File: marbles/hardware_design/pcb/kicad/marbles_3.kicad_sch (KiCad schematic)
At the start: 39 parts

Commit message: replace led/button switches
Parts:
- removed SW1, SW2: (no value), symbol marbles-eagle-import:LP4OA1PBCT
- added SW1, SW2: SW_Push_LED, Supercell 1.3:C&K_D6R, symbol Switch:SW_Push_LED
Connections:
- net GND: now also SW1.1, SW1.2, SW2.1, SW2.2
- net SW_T_DV: now also SW1.4
- net SW_X_DV: now also SW2.4
- net at R1.2: now also SW1.3
- net at R5.2: now also SW2.3
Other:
- moved on the sheet: R1, R5

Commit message: added SMD LEDs in parallel with THT footprint
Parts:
- removed LED1, LED2, LED3, LED4, LED5: (no value), symbol marbles-eagle-import:LED-BICOLOR-THROUGHHOLE2.54
- added LED1, LED2, LED3, LED4, LED5: LED-BICOLOR-THROUGHHOLE, marbles:LED-BICOLOR-THROUGHHOLE-2.54, symbol marbles-eagle-import:LED-BICOLOR-THROUGHHOLE
- added LED1-2, LED2-2, LED3-2, LED4-2, LED5-2: LED_Dual_KAKA, Supercell 1.3:bicolor 0606 LED, symbol Device:LED_Dual_KAKA
- C17, C18, C24, C28, C29, C36, C38, C8: value (none) -> 100n; footprint (none) -> marbles:C0402
- R1, R5: value (none) -> 39; footprint (none) -> marbles:R0402
- R10, R12, R17, R18, R36: value (none) -> 1.5k; footprint (none) -> marbles:R0402
- R11, R15, R19, R9: value (none) -> 2.2k; footprint (none) -> marbles:R0402
- R13, R14, R16, R20, R21, R37, R38, R4: value (none) -> 10kB; footprint (none) -> marbles:ALPS_POT_VERTICAL_PS
- SW3, SW4, SW5, SW6, SW7: value (none) -> TAC_SWITCHPTH; footprint (none) -> marbles:TACTILE-PTH
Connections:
- net GND: now also LED1-2.KG, LED1-2.KR, LED1.2 (C), LED2-2.KG, LED2-2.KR, LED2.2 (C), LED3-2.KG, LED3-2.KR, LED3.2 (C), LED4-2.KG, LED4-2.KR, LED4.2 (C), LED5-2.KG, LED5.2 (C)
- net at R9.2: now also LED1-2.AR, LED1.3 (RED)
- net at R15.2: now also LED4-2.AR, LED4.3 (RED)
- net at R17.2: now also LED4-2.AG, LED4.1 (GRN)
- net at R36.2: now also LED5-2.AG, LED5.1 (GRN)
- net at R12.2: now also LED2-2.AG, LED2.1 (GRN)
- net at R11.2: now also LED2-2.AR, LED2.3 (RED)
- net at R10.2: now also LED1-2.AG, LED1.1 (GRN)
- net at R18.2: now also LED3-2.AG, LED3.1 (GRN)
- net at R19.2: now also LED3-2.AR, LED3.3 (RED)
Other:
- moved on the sheet: R10, R11, R12, R15, R17, R18, R19, R36, R9

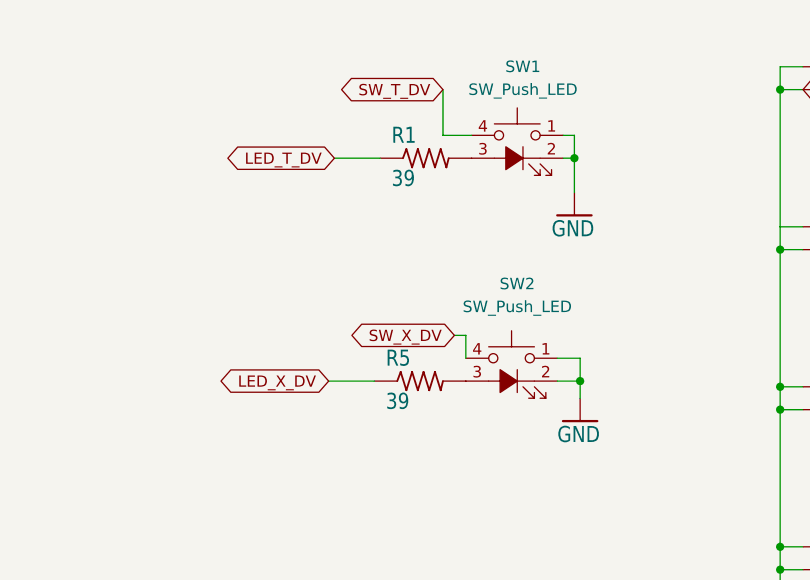
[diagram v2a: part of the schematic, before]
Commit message: change two 39 ohm 0402 resistors to 1k 0603
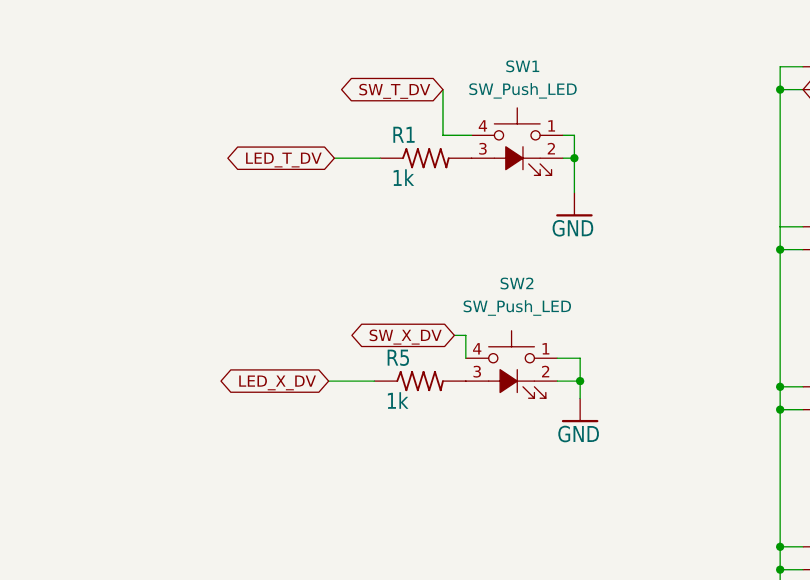
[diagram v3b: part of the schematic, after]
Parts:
- R1, R5: value 39 -> 1k; footprint marbles:R0402 -> marbles:R0603
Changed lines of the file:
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@@
       (effects (font (size 1.778 1.5113)) (justify left bottom))
     )
-    (property "Value" "39" (id 1) (at 142.24 163.322 0)
-      (effects (font (size 1.778 1.5113)) (justify left bottom))
-    )
-    (property "Footprint" "marbles:R0402" (id 2) (at 146.05 160.02 0)
+    (property "Value" "1k" (id 1) (at 142.24 163.322 0)
+      (effects (font (size 1.778 1.5113)) (justify left bottom))
+    )
+    (property "Footprint" "marbles:R0603" (id 2) (at 146.05 160.02 0)
       (effects (font (size 1.27 1.27)) hide)
     )
@@
       (effects (font (size 1.778 1.5113)) (justify left bottom))
     )
-    (property "Value" "39" (id 1) (at 141.605 188.087 0)
-      (effects (font (size 1.778 1.5113)) (justify left bottom))
-    )
-    (property "Footprint" "marbles:R0402" (id 2) (at 145.415 184.785 0)
-      (effects (font (size 1.27 1.27)) hide)
-    )
+    (property "Value" "1k" (id 1) (at 141.605 188.087 0)
+      (effects (font (size 1.778 1.5113)) (justify left bottom))
+    )
+    (property "Footprint" "marbles:R0603" (id 2) (at 145.415 184.785 0)
+      (effects (font (size 1.27 1.27)) hide)
+    )

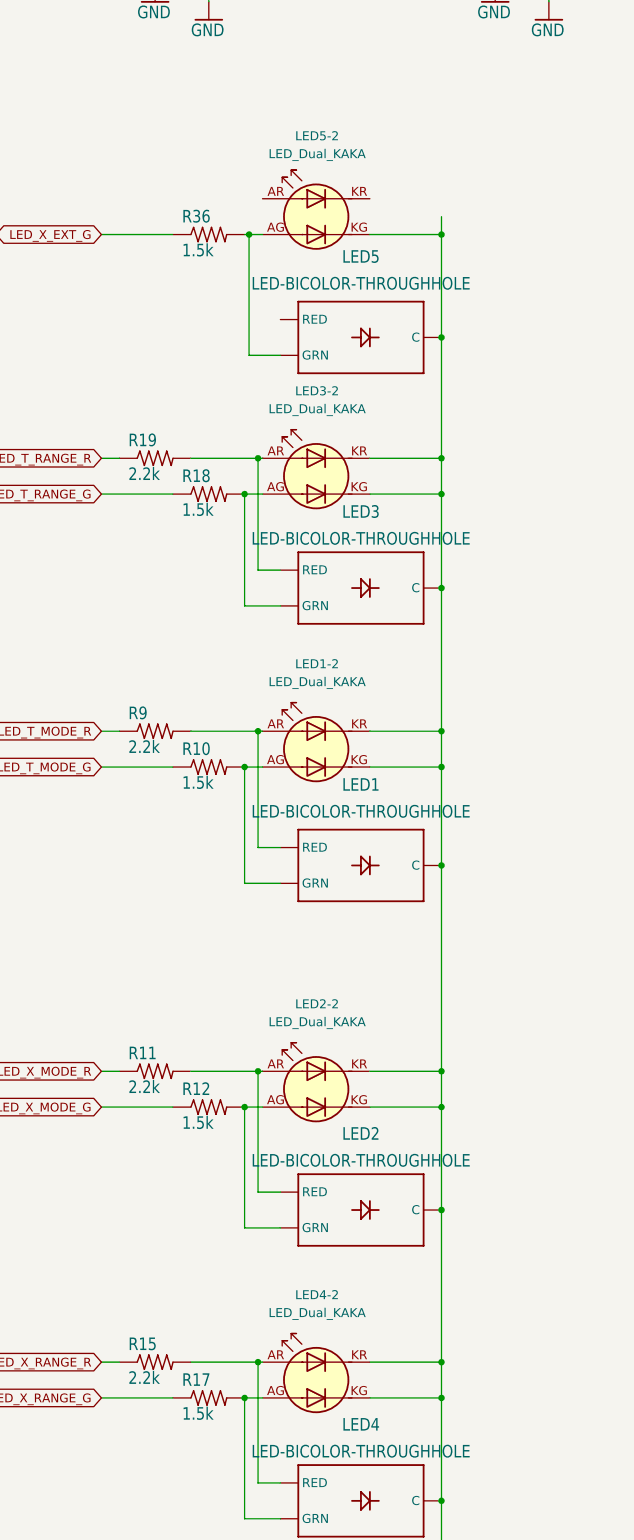
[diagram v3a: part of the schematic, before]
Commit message: marbles remove SMD LEDs, revert to THT
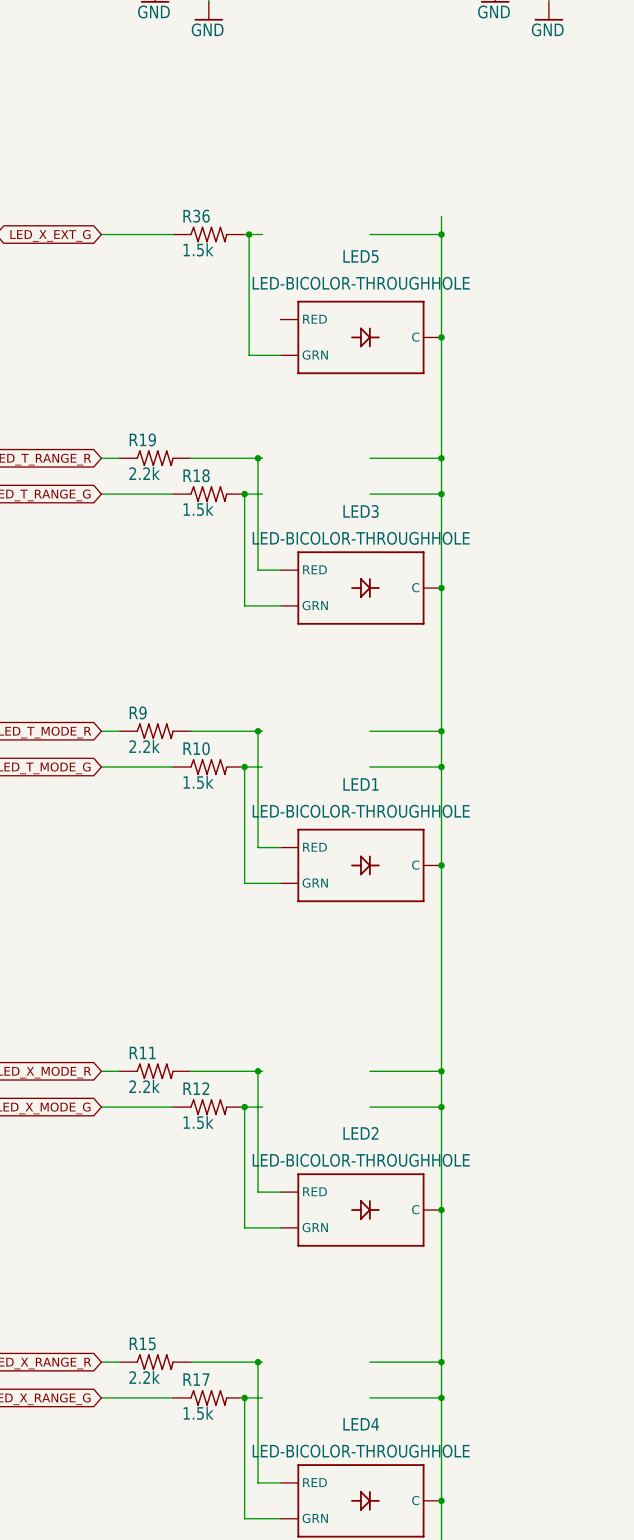
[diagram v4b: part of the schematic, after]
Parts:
- removed LED1-2, LED2-2, LED3-2, LED4-2, LED5-2: LED_Dual_KAKA, Supercell 1.3:bicolor 0606 LED, symbol Device:LED_Dual_KAKA
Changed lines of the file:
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@@
     (pin "2")
-  )
-  (symbol (lib_name "LED_Dual_KAKA_2") (lib_id "Device:LED_Dual_KAKA") (at 292.1 276.225 0) (mirror y) (unit 1)
-    (in_bom yes) (on_board yes) (fields_autoplaced)
-    (property "Reference" "LED2-2" (id 0) (at 292.227 264.16 0))
-    (property "Value" "LED_Dual_KAKA" (id 1) (at 292.227 266.7 0))
-    (property "Footprint" "Supercell 1.3:bicolor 0606 LED" (id 2) (at 291.338 276.225 0)
-      (effects (font (size 1.27 1.27)) hide)
-    )
-    (property "Datasheet" "~" (id 3) (at 291.338 276.225 0)
-      (effects (font (size 1.27 1.27)) hide)
-    )
-    (pin "AG")
-    (pin "AR")
-    (pin "KG")
-    (pin "KR")
   )
   (symbol (lib_id "marbles-eagle-import:POT_USVERTICAL_PS") (at 78.74 109.22 0) (unit 1)
@@
     (pin "P$3")
   )
-  (symbol (lib_name "LED_Dual_KAKA_1") (lib_id "Device:LED_Dual_KAKA") (at 292.1 317.5 0) (mirror y) (unit 1)
-    (in_bom yes) (on_board yes) (fields_autoplaced)
-    (property "Reference" "LED4-2" (id 0) (at 292.227 305.435 0))
-    (property "Value" "LED_Dual_KAKA" (id 1) (at 292.227 307.975 0))
-    (property "Footprint" "Supercell 1.3:bicolor 0606 LED" (id 2) (at 291.338 317.5 0)
-      (effects (font (size 1.27 1.27)) hide)
-    )
-    (property "Datasheet" "~" (id 3) (at 291.338 317.5 0)
-      (effects (font (size 1.27 1.27)) hide)
-    )
-    (pin "AG")
-    (pin "AR")
-    (pin "KG")
-    (pin "KR")
-  )
   (symbol (lib_id "marbles-eagle-import:LED-BICOLOR-THROUGHHOLE") (at 297.18 334.645 0) (unit 1)
     (in_bom yes) (on_board yes) (fields_autoplaced)
@@
     (pin "2")
   )
-  (symbol (lib_name "LED_Dual_KAKA_3") (lib_id "Device:LED_Dual_KAKA") (at 292.1 189.23 0) (mirror y) (unit 1)
-    (in_bom yes) (on_board yes) (fields_autoplaced)
-    (property "Reference" "LED3-2" (id 0) (at 292.227 177.165 0))
-    (property "Value" "LED_Dual_KAKA" (id 1) (at 292.227 179.705 0))
-    (property "Footprint" "Supercell 1.3:bicolor 0606 LED" (id 2) (at 291.338 189.23 0)
-      (effects (font (size 1.27 1.27)) hide)
-    )
-    (property "Datasheet" "~" (id 3) (at 291.338 189.23 0)
-      (effects (font (size 1.27 1.27)) hide)
-    )
-    (pin "AG")
-    (pin "AR")
-    (pin "KG")
-    (pin "KR")
-  )
   (symbol (lib_id "marbles-eagle-import:LED-BICOLOR-THROUGHHOLE") (at 297.18 169.545 0) (unit 1)
     (in_bom yes) (on_board yes) (fields_autoplaced)
@@
     (pin "1")
   )
-  (symbol (lib_name "LED_Dual_KAKA_4") (lib_id "Device:LED_Dual_KAKA") (at 292.1 152.4 0) (mirror y) (unit 1)
-    (in_bom yes) (on_board yes) (fields_autoplaced)
-    (property "Reference" "LED5-2" (id 0) (at 292.227 140.97 0))
-    (property "Value" "LED_Dual_KAKA" (id 1) (at 292.227 143.51 0))
-    (property "Footprint" "Supercell 1.3:bicolor 0606 LED" (id 2) (at 291.338 152.4 0)
-      (effects (font (size 1.27 1.27)) hide)
-    )
-    (property "Datasheet" "~" (id 3) (at 291.338 152.4 0)
-      (effects (font (size 1.27 1.27)) hide)
-    )
-    (pin "AG")
-    (pin "AR")
-    (pin "KG")
-    (pin "KR")
-  )
   (symbol (lib_id "marbles-eagle-import:LED-BICOLOR-THROUGHHOLE") (at 297.18 293.37 0) (unit 1)
     (in_bom yes) (on_board yes) (fields_autoplaced)
@@
     (pin "1")
   )
-  (symbol (lib_id "Device:LED_Dual_KAKA") (at 292.1 227.965 0) (mirror y) (unit 1)
-    (in_bom yes) (on_board yes) (fields_autoplaced)
-    (property "Reference" "LED1-2" (id 0) (at 292.227 215.9 0))
-    (property "Value" "LED_Dual_KAKA" (id 1) (at 292.227 218.44 0))
-    (property "Footprint" "Supercell 1.3:bicolor 0606 LED" (id 2) (at 291.338 227.965 0)
-      (effects (font (size 1.27 1.27)) hide)
-    )
-    (property "Datasheet" "~" (id 3) (at 291.338 227.965 0)
-      (effects (font (size 1.27 1.27)) hide)
-    )
-    (pin "AG")
-    (pin "AR")
-    (pin "KG")
-    (pin "KR")
-  )
   (symbol (lib_id "marbles-eagle-import:R-US_R0402") (at 276.86 191.77 0) (unit 1)

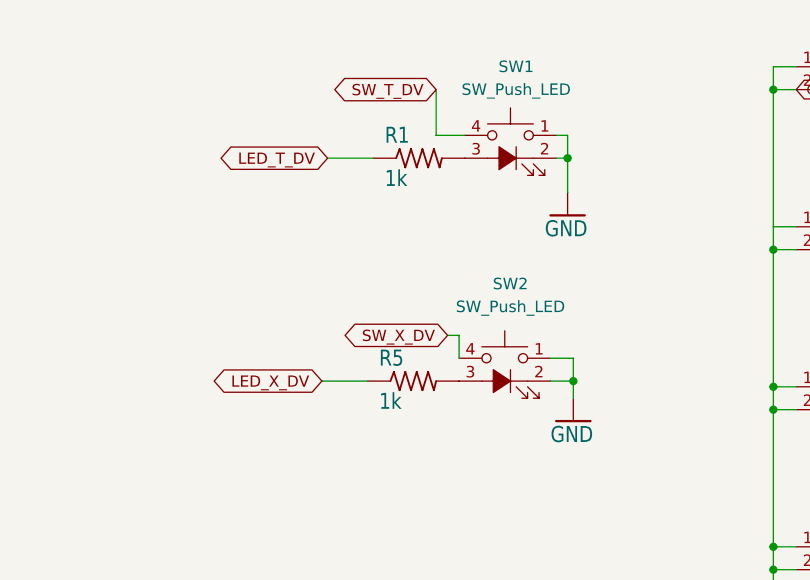
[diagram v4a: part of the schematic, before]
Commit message: marbles change button LEDs from 1k to 680R
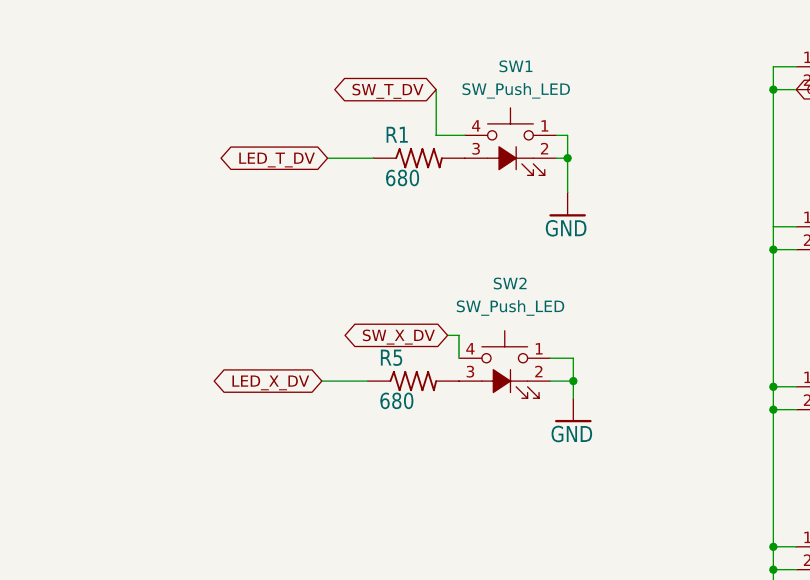
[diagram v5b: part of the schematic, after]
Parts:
- R1, R5: value 1k -> 680
